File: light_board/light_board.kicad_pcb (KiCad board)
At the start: 2 copper layers, 37.5 x 35 mm, 17 parts, among them J1 CONN_01X02, J2 Screw_Terminal_1x02, J3 Screw_Terminal_1x02, Q1 FDC658AP, U1 LM3409MY

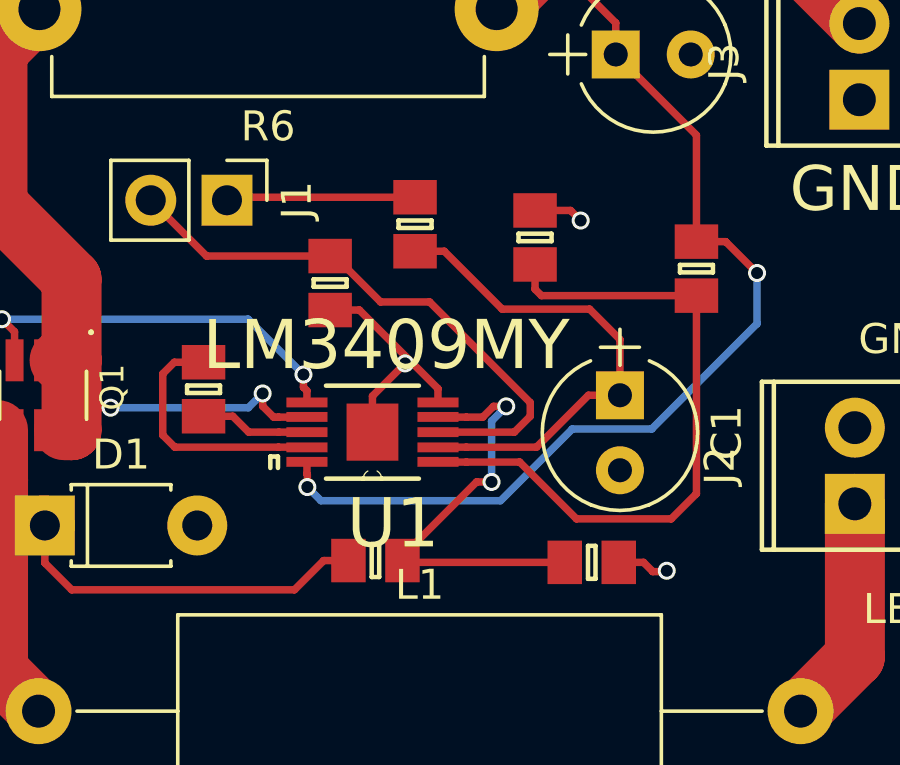
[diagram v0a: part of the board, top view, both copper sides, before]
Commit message: Made sure to commit all the resistor changes to the footprint that we already own
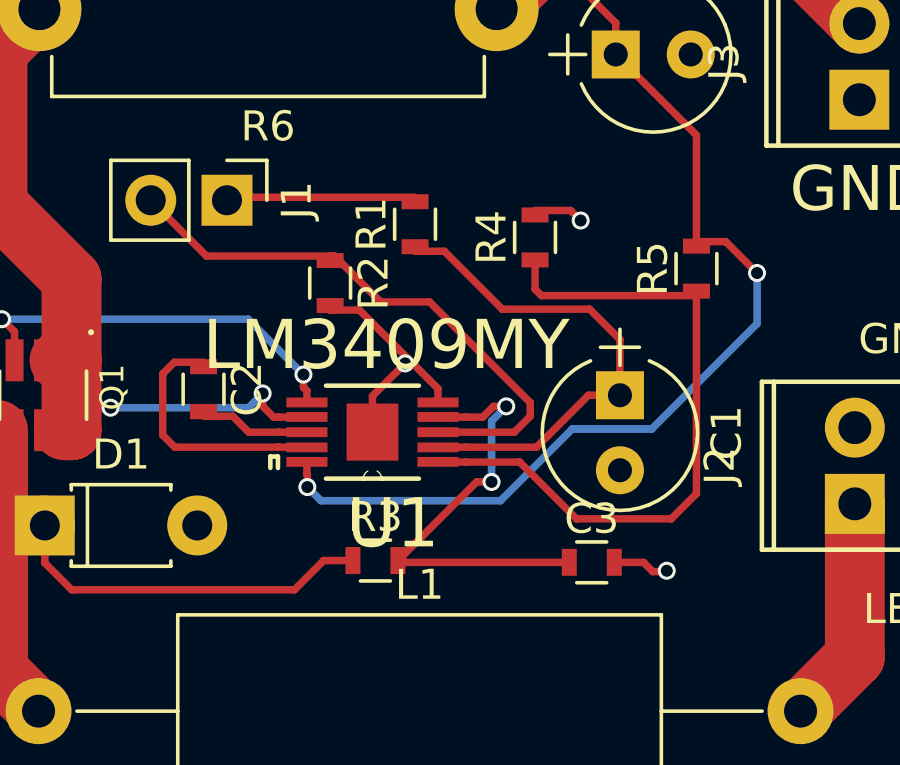
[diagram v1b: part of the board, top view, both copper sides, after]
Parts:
- C2, C3, R1, R2, R3, R4, R5: footprint agg:0805 -> Resistors_SMD:R_0603

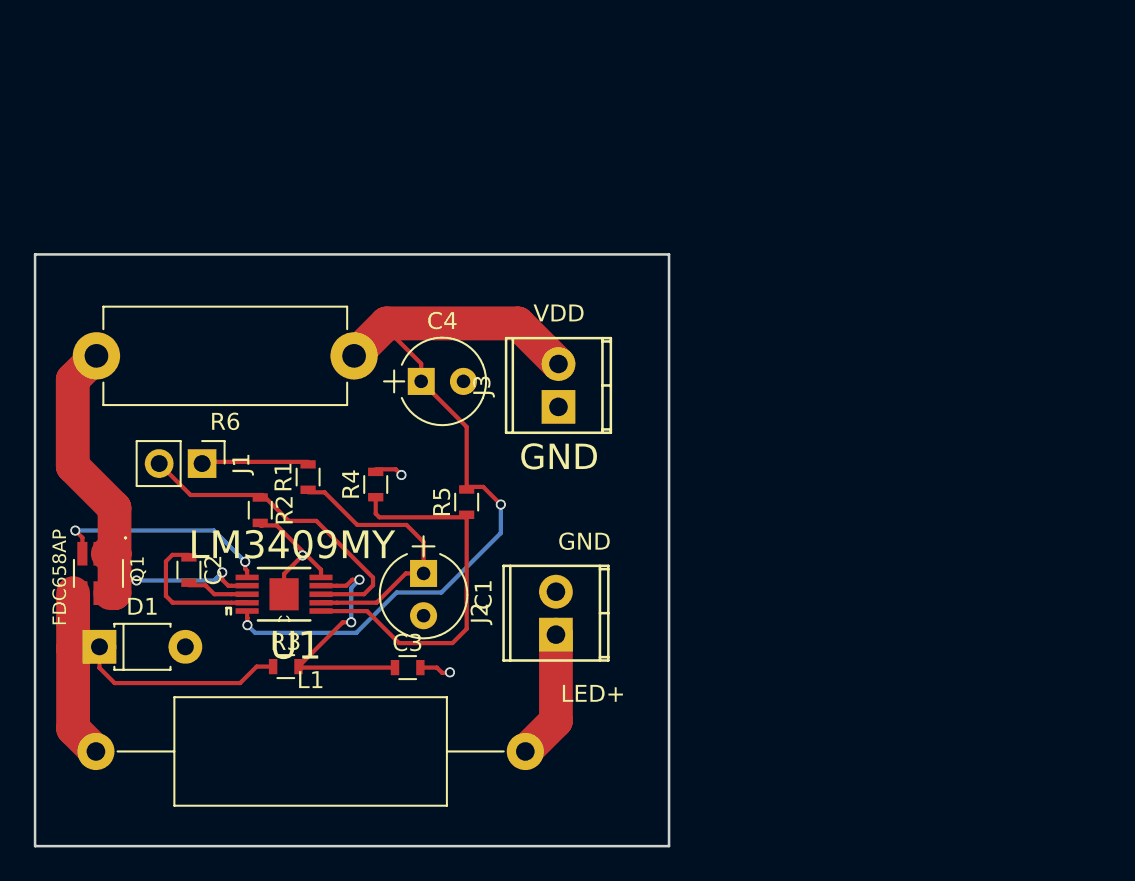
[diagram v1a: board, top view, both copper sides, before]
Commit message: added mounting holes and changed light board footprints
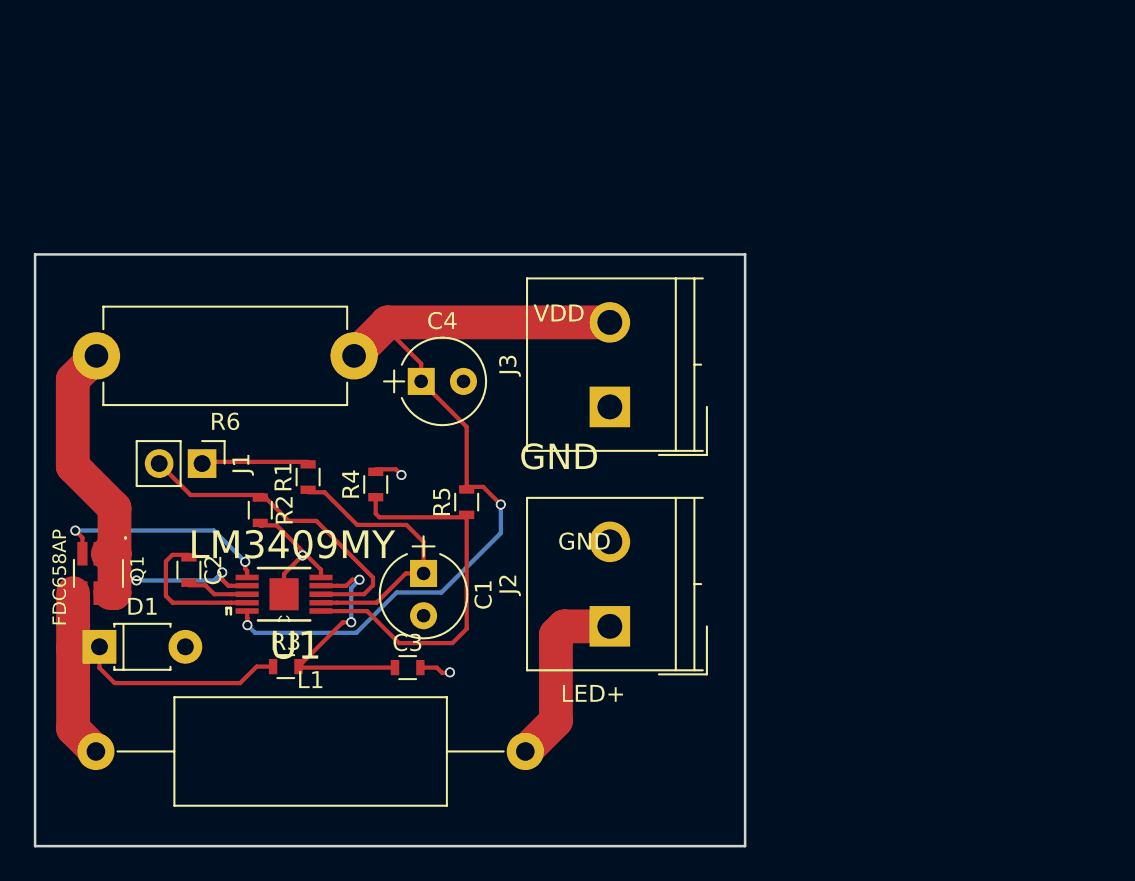
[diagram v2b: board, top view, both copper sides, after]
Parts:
- J2: value Screw_Terminal_1x02 -> Led_Connector; footprint footprints:POWER_CONN -> Connectors_Terminal_Blocks:TerminalBlock_Philmore_TB132_02x5mm_Straight
- J3: value Screw_Terminal_1x02 -> Power_Connector; footprint footprints:POWER_CONN -> Connectors_Terminal_Blocks:TerminalBlock_Philmore_TB132_02x5mm_Straight
- moved J2 3.23 mm to (174.0, 127.0)
- moved J3 3.04 mm to (174.0, 114.0)
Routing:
- net Net-(J2-Pad1): track 7.66 -> 11.1 mm
- net /CSP: track 51.8 -> 53.9 mm
- removed copper zone on B.Cu, net GND
- removed copper zone on F.Cu, net GND
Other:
- board size 37.5 x 35 mm -> 42 x 35 mm

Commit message: finished wiring pcb
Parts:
- removed C1: 1uF, Capacitors_THT:CP_Radial_Tantal_D5.0mm_P2.50mm
- removed C2: 1uF, Resistors_SMD:R_0603
- removed C3: 1nF, Resistors_SMD:R_0603
- removed C4: 30uF, Capacitors_THT:CP_Radial_Tantal_D5.0mm_P2.50mm
- removed R1: 1K, Resistors_SMD:R_0603
- removed R2: 4.7K, Resistors_SMD:R_0603
- removed R3: 3K9, Resistors_SMD:R_0603
- removed R4: 1K8, Resistors_SMD:R_0603
- removed R5: 15K, Resistors_SMD:R_0603
- removed R6: 0.1R, Resistors_THT:R_Axial_DIN0614_L14.3mm_D5.7mm_P15.24mm_Horizontal
- added Cf1: 1uF, Capacitors_SMD:C_0603, F.Cu at (166.4, 97.8)
- added Cin1: 5uF, Capacitors_SMD:C_0603, F.Cu at (176.5, 97.8)
- added Coff1: 470pF, Capacitors_SMD:C_0603, F.Cu at (176.5, 104.1)
- added D2: LED, LEDs:LED_0603, F.Cu at (158.8, 111.8)
- added Rled1: 1kR, Resistors_SMD:R_0603, F.Cu at (165.1, 111.8)
- added Roff1: 13k, Resistors_SMD:R_0603, F.Cu at (176.5, 111.8)
- added Rsns1: 0.15R, Resistors_SMD:R_0603, F.Cu at (171.4, 97.8)
- added Ruv1: 6K49, Resistors_SMD:R_0603, F.Cu at (157.5, 97.8)
- added Ruv2: 73K2, Resistors_SMD:R_0603, F.Cu at (161.3, 97.8)
- D1: footprint Diodes_THT:D_T-1_P5.08mm_Horizontal -> Diodes_SMD:D_0603
- J1: footprint Pin_Headers:Pin_Header_Straight_1x02_Pitch2.54mm -> Connectors_Terminal_Blocks:TerminalBlock_Pheonix_MPT-2.54mm_2pol
- J2, J3: footprint Connectors_Terminal_Blocks:TerminalBlock_Philmore_TB132_02x5mm_Straight -> Connectors_Terminal_Blocks:TerminalBlock_Pheonix_PT-3.5mm_2pol
- L1: value 15uH -> 12.5uH
- Q1: footprint footprints:SOT95P280X110-6N -> footprints:FDC658AP_FDC658AP
- moved Q1 29.1 mm to (170.2, 111.8), turned to 180 degrees
- moved U1 25.3 mm to (168.9, 104.1), turned to 0 degrees
- moved L1 23.2 mm to (161.3, 119.4)
- moved J2 17.6 mm to (182.9, 111.8)
- moved D1 16.0 mm to (156.2, 118.1), turned to 90 degrees
- moved J3 15.3 mm to (182.9, 101.6)
- moved J1 14.9 mm to (158.8, 105.4), turned to 90 degrees
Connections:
- net Net-(J1-Pad2) renamed /inputSignal
- net Net-(J2-Pad1) renamed /LEDVcc
- D1 pad 1: Net-(D1-Pad1) -> /diodeToLToPMOS
- J1 pad 1: Net-(J1-Pad1) -> /notUsed
- L1 pad 1: Net-(D1-Pad1) -> /diodeToLToPMOS
- Q1 pad 1: /CSN -> /diodeToLToPMOS
- Q1 pad 2: /CSN -> /diodeToLToPMOS
- Q1 pad 4: Net-(D1-Pad1) -> /CSN
- Q1 pad 5: /CSN -> /diodeToLToPMOS
- Q1 pad 6: /CSN -> /diodeToLToPMOS
- U1 pad 2: Net-(C1-Pad1) -> /notUsed
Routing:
- net GND: track 11.8 -> 76.4 mm, vias 3 -> 2
- net /CSP: track 53.9 -> 29.0 mm, vias 2 -> 0
- net Net-(D1-Pad1): track 23.7 -> 0.00 mm
- net /diodeToLToPMOS: track 0.00 -> 20.0 mm
- net /notUsed: track 0.00 -> 19.5 mm
- net Net-(C1-Pad1): track 16.7 -> 0.00 mm
- net /COFF: track 14.7 -> 28.4 mm
- net /UVLO: track 22.6 -> 11.5 mm
- net /inputSignal: track 19.2 -> 8.50 mm
- net Net-(J1-Pad1): track 6.31 -> 0.00 mm
- net Net-(D2-Pad2): track 0.00 -> 5.86 mm
- net /LEDVcc: track 11.1 -> 15.9 mm
- net /PGATE: track 13.3 -> 17.9 mm, vias 2 -> 0
- net /CSN: track 25.2 -> 21.7 mm
- net Net-(Cf1-Pad1): track 8.54 -> 11.9 mm, vias 0 -> 2
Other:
- board outline removed
- net class Default: trace_width 0.25 -> 0.2
- rule pad_to_mask_clearance: 0.2 -> 0
- board text removed: "GND"
- board text removed: "LED+"
- board text removed: "VDD"

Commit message: light_board finished
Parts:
- D1: footprint Diodes_SMD:D_0603 -> Diodes_THT:D_T-1_P5.08mm_Horizontal
- moved D1 36.2 mm to (184.8, 95.9), turned to 270 degrees
- moved Ruv1 34.4 mm to (184.8, 118.7), turned to 270 degrees
- moved L1 29.7 mm to (181.0, 97.2), turned to 180 degrees
- moved Ruv2 28.8 mm to (181.0, 118.7), turned to 270 degrees
- moved J3 27.0 mm to (159.4, 114.9), turned to 270 degrees
- moved J1 26.9 mm to (184.2, 114.3)
- moved D2 25.7 mm to (183.5, 104.8), turned to 180 degrees
- moved J2 24.5 mm to (159.4, 104.8), turned to 270 degrees
- moved Cin1 23.6 mm to (165.7, 118.7), turned to 90 degrees
- moved Cf1 23.0 mm to (175.9, 118.7), turned to 270 degrees
- moved Rsns1 21.0 mm to (170.8, 118.7), turned to 90 degrees
- moved Rled1 13.9 mm to (177.2, 104.8), turned to 270 degrees
- moved Coff1 13.6 mm to (165.7, 112.4), turned to 270 degrees
- moved Roff1 12.9 mm to (165.7, 104.8), turned to 270 degrees
- moved U1 9.38 mm to (173.4, 112.4), turned to 180 degrees
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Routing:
- net /notUsed: track 19.5 -> 9.19 mm
- net GND: track 76.4 -> 74.2 mm
- net Net-(Cf1-Pad1): track 11.9 -> 13.9 mm
- net /diodeToLToPMOS: track 20.0 -> 19.1 mm
- net /inputSignal: track 8.50 -> 9.23 mm
- added copper zone on F.Cu, net /inputSignal

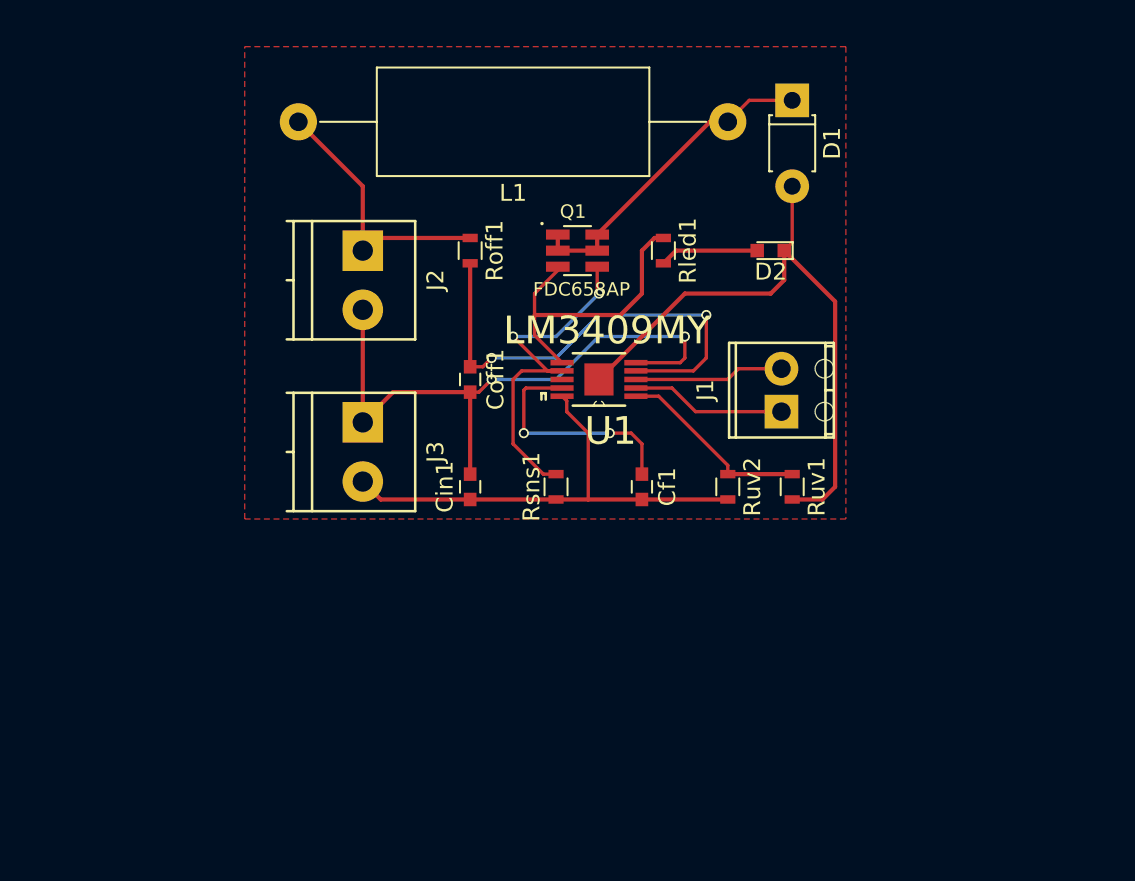
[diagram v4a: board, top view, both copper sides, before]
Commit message: changed footprints of resistor and diode
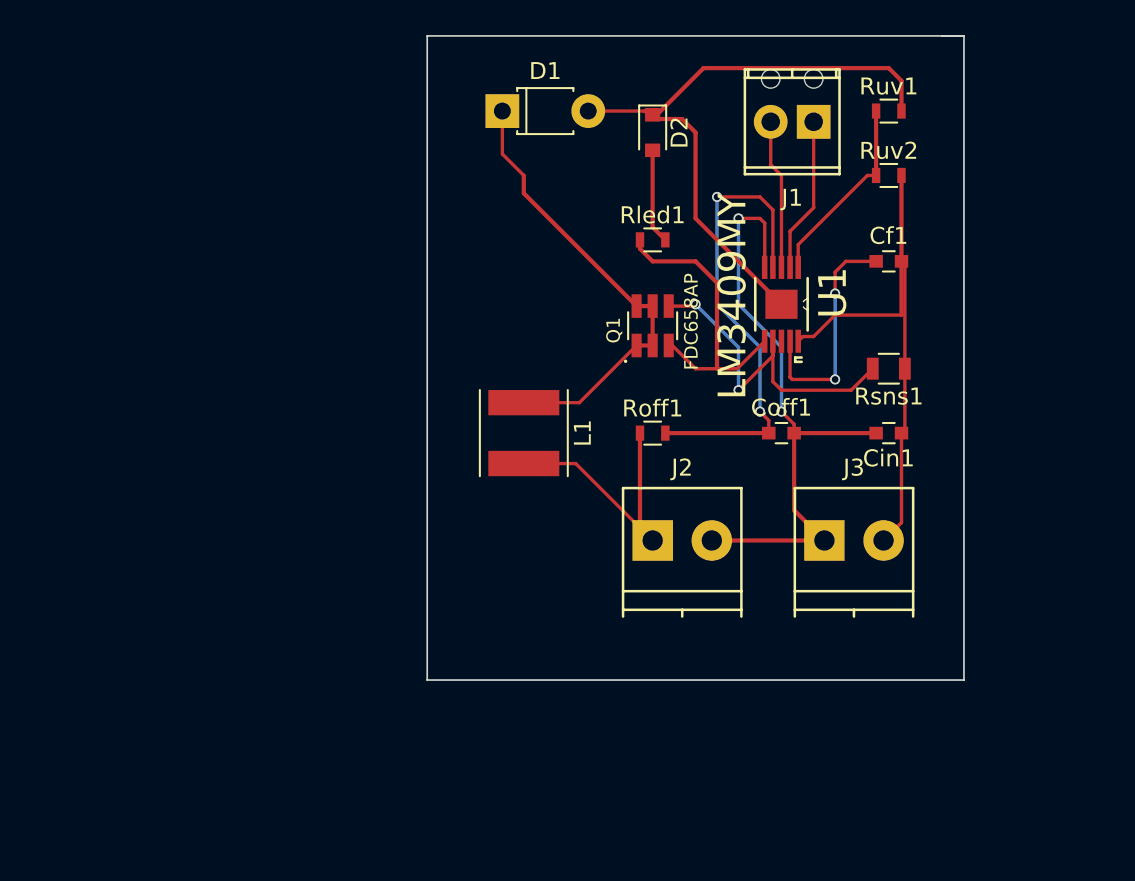
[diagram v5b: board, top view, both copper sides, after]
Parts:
- D2: footprint LEDs:LED_0603 -> Diodes_SMD:D_0805
- L1: footprint Inductors_THT:L_Axial_L16.0mm_D6.3mm_P25.40mm_Horizontal_Fastron_VHBCC -> Inductors_SMD:L_Taiyo-Yuden_MD-5050
- Rsns1: footprint Resistors_SMD:R_0603 -> Resistors_SMD:R_0805
- moved J3 28.2 mm to (186.7, 121.9), turned to 0 degrees
- moved Cin1 25.0 mm to (190.5, 115.6), turned to 180 degrees
- moved J2 24.2 mm to (176.5, 121.9), turned to 0 degrees
- moved Ruv1 22.9 mm to (190.5, 96.5), turned to 0 degrees
- moved L1 22.0 mm to (168.9, 115.6), turned to 270 degrees
- moved Rsns1 20.9 mm to (190.5, 111.8), turned to 180 degrees
- moved Ruv2 20.7 mm to (190.5, 100.3), turned to 0 degrees
- moved Cf1 19.8 mm to (190.5, 105.4), turned to 0 degrees
- moved Coff1 18.7 mm to (184.2, 115.6), turned to 0 degrees
- moved J1 17.3 mm to (186.1, 97.2), turned to 180 degrees
- moved D1 17.2 mm to (167.6, 96.5), turned to 0 degrees
- moved Roff1 15.3 mm to (176.5, 115.6), turned to 0 degrees
- moved U1 11.7 mm to (184.2, 108.0), turned to 270 degrees
- moved D2 9.88 mm to (176.5, 97.8), turned to 270 degrees
- moved Q1 6.29 mm to (176.5, 109.2), turned to 90 degrees
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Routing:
- net /diodeToLToPMOS: track 19.1 -> 27.1 mm
- net /CSP: track 28.8 -> 32.4 mm
- net /CSN: track 21.7 -> 20.5 mm
- removed copper zone on F.Cu, net /inputSignal
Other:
- board outline added: 31.8 x 38.1 mm
- net class wide added: clearance 0.2, trace_width 2, via_dia 0.6, via_drill 0.4

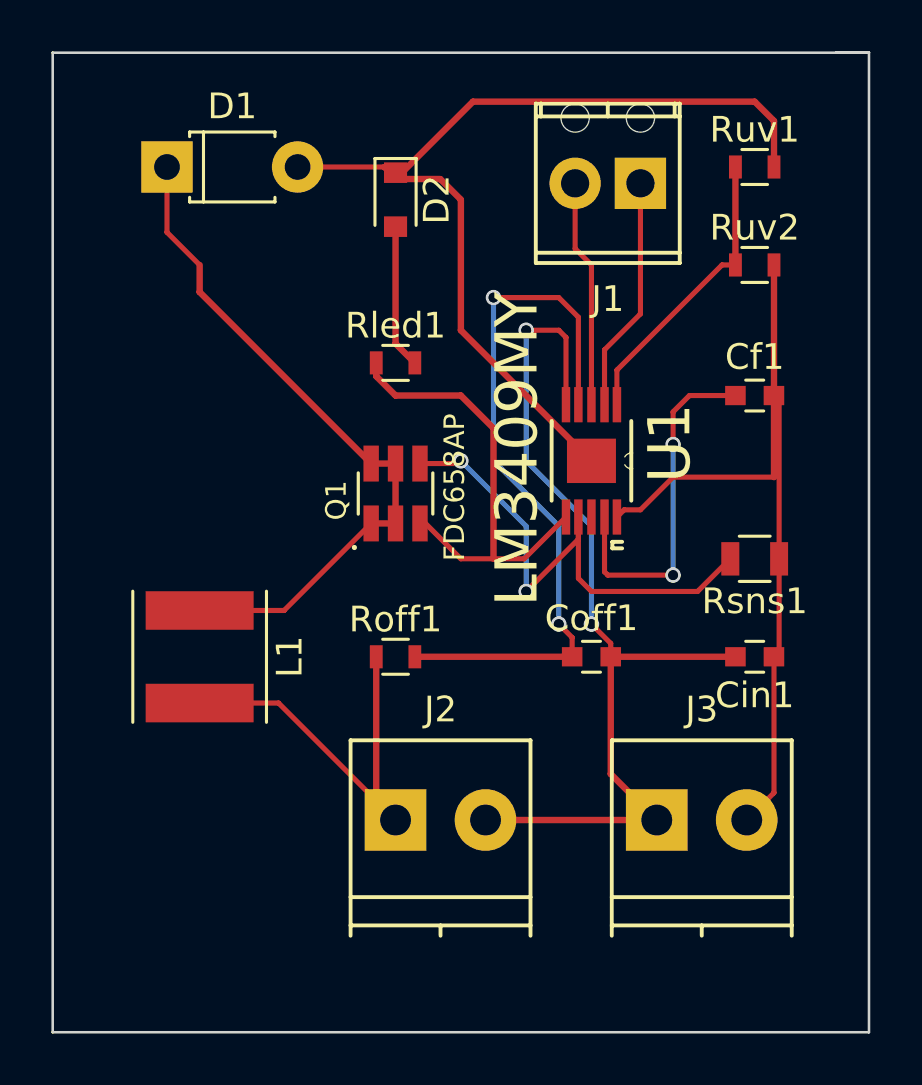
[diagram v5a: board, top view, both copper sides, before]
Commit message: light board finished - added ground plane and thick tracks
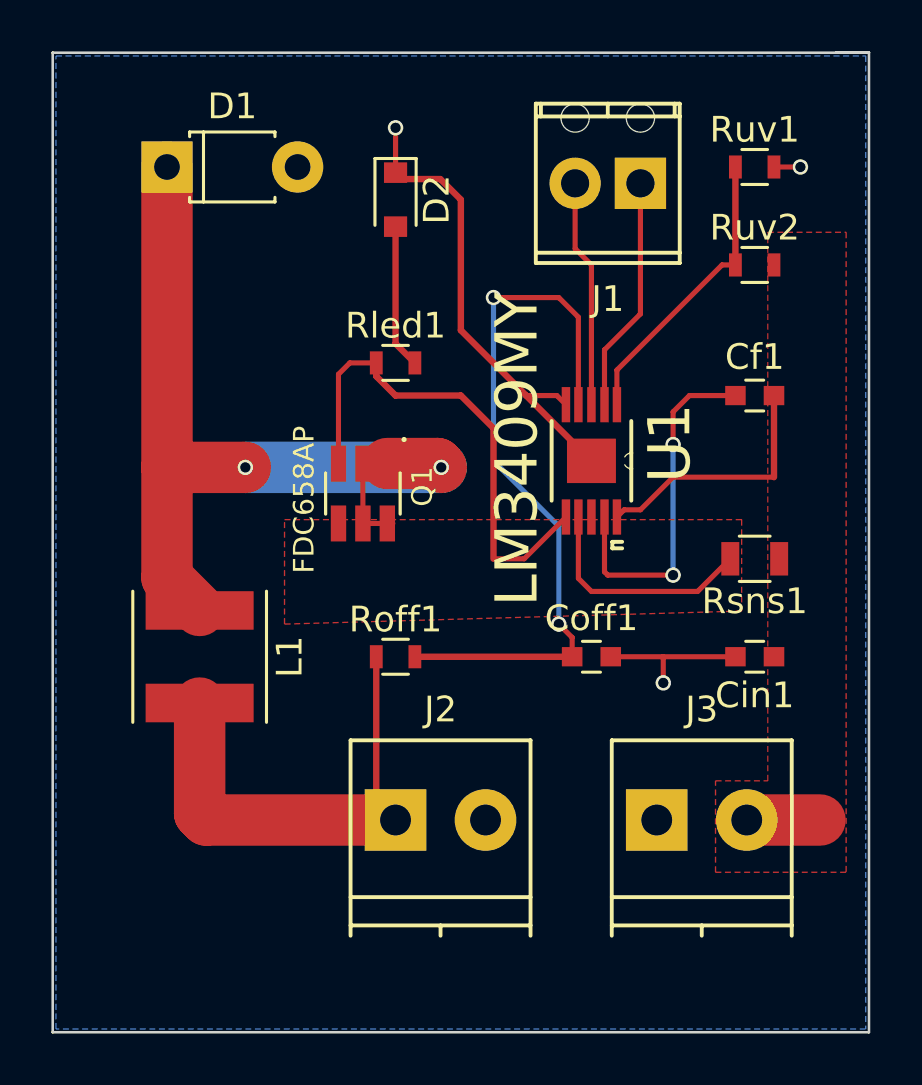
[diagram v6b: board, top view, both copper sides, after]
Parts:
- Cin1: value 5uF -> 4u7F
- Roff1: value 13k -> 12k
- moved Q1 1.27 mm to (175.3, 109.2), turned to 270 degrees
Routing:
- net GND: track 74.2 -> 25.5 mm, vias 2 -> 3
- net /CSP: track 32.4 -> 13.7 mm
- net /CSN: track 20.5 -> 9.03 mm, vias 2 -> 0
- net /diodeToLToPMOS: track 27.1 -> 36.1 mm, vias 0 -> 2
- net /LEDVcc: track 16.2 -> 18.7 mm
- net /PGATE: track 17.9 -> 19.6 mm
- added copper zone on F.Cu, net /CSN
- added copper zone on F.Cu, net /CSP
- added copper zone on B.Cu, net GND
